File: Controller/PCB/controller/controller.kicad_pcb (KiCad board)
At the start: 2 copper layers, 99.1 x 99.1 mm, 64 parts, among them J1 nRF24L01_Conn, Q1 S9013, Q2 S9013, Q3 S9013, SW1 SW_SPDT, U1 Joystick, U2 Joystick, U3 ZSR330GTA, U4 LM358DR2G, U5 ZLDO1117G50TA

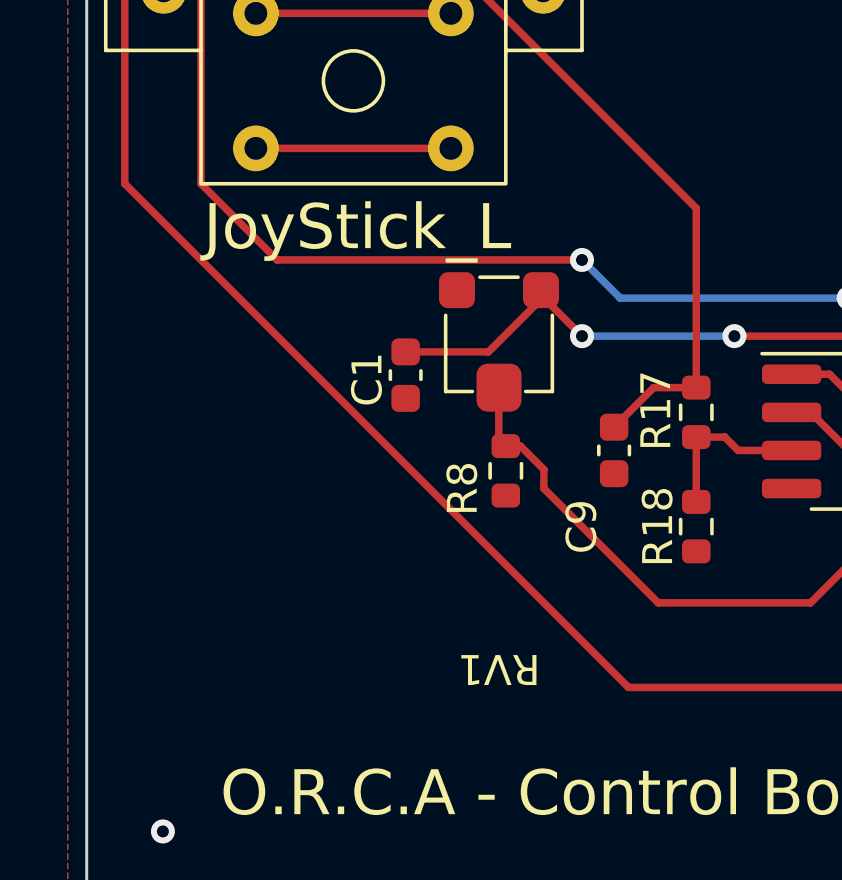
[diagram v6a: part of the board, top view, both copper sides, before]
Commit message: Change footprint of RV1 and update gerber files
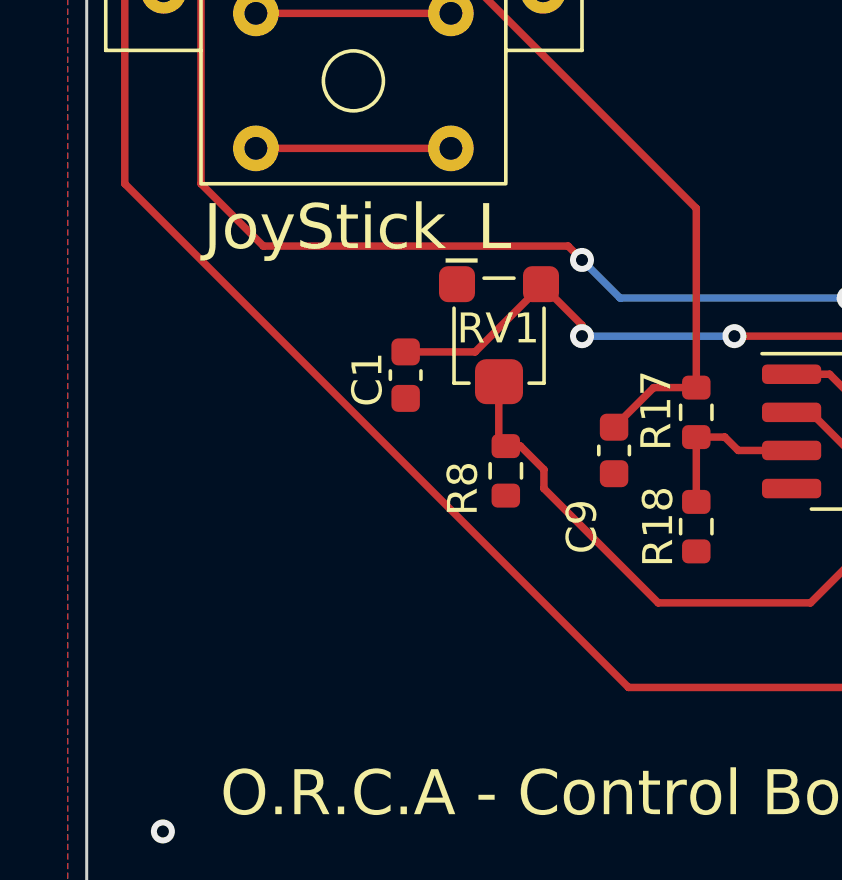
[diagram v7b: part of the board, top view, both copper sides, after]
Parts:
- RV1: footprint My_library:35WR100KLFTR -> My_library:Variable_Resistor
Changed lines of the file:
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@@
     )
   )
-  (footprint "My_library:35WR100KLFTR" (layer "F.Cu")
+  (footprint "My_library:Variable_Resistor" (layer "F.Cu")
     (at 120.423906 130.877391 180)
     (property "Sheetfile" "controller.kicad_sch")
     (property "Sheetname" "")
     (attr smd)
-    (fp_text reference "RV1" (at 0 -11.025 180 unlocked) (layer "F.SilkS")
-      (effects (font (size 1 1) (thickness 0.15)))
-    )
-    (fp_text value "20K" (at 0 -9.525 180 unlocked) (layer "F.Fab")
-      (effects (font (size 1 1) (thickness 0.15)))
-    )
-    (fp_text user "${REFERENCE}" (at 0 -7.62 180 unlocked) (layer "F.Fab")
-      (effects (font (size 1 1) (thickness 0.15)))
-    )
-    (fp_line (start -1.778 -1.778) (end -1.778 0.762) (layer "F.SilkS") (width 0.12))
-    (fp_line (start -0.889 -1.778) (end -1.778 -1.778) (layer "F.SilkS") (width 0.12))
-    (fp_line (start 0.889 -1.778) (end 1.778 -1.778) (layer "F.SilkS") (width 0.12))
-    (fp_line (start -0.635 2.032) (end 0.635 2.032) (layer "F.SilkS") (width 0.12))
-    (fp_line (start 1.778 -1.778) (end 1.778 0.762) (layer "F.SilkS") (width 0.12))
-    (pad "1" smd roundrect (at -1.4 1.6 180) (size 1.2 1.2) (layers "F.Cu" "F.Paste" "F.Mask") (roundrect_rratio 0.25)
+    (fp_text reference "RV1" (at 0.027906 0.321391 unlocked) (layer "F.SilkS")
+      (effects (font (size 1 1) (thickness 0.15)))
+    )
+    (fp_text value "20K" (at 0 -10.5 180 unlocked) (layer "F.Fab")
+      (effects (font (size 1 1) (thickness 0.15)))
+    )
+    (fp_text user "${REFERENCE}" (at 0 -9 180 unlocked) (layer "F.Fab")
+      (effects (font (size 1 1) (thickness 0.15)))
+    )
+    (fp_line (start 1.5 -1.5) (end 1.5 1) (layer "F.SilkS") (width 0.12))
+    (fp_line (start 0.5 2) (end -0.5 2) (layer "F.SilkS") (width 0.12))
+    (fp_line (start -1.5 1) (end -1.5 -1.5) (layer "F.SilkS") (width 0.12))
+    (fp_line (start 1 -1.5) (end 1.5 -1.5) (layer "F.SilkS") (width 0.12))
+    (fp_line (start -1.5 -1.5) (end -1 -1.5) (layer "F.SilkS") (width 0.12))
+    (pad "1" smd roundrect (at -1.4 1.8 180) (size 1.2 1.2) (layers "F.Cu" "F.Paste" "F.Mask") (roundrect_rratio 0.25)
       (net 19 "+5V") (pinfunction "1") (pintype "passive"))
-    (pad "2" smd roundrect (at 0 -1.65 180) (size 1.5 1.6) (layers "F.Cu" "F.Paste" "F.Mask") (roundrect_rratio 0.25)
+    (pad "2" smd roundrect (at 0 -1.45 180) (size 1.6 1.5) (layers "F.Cu" "F.Paste" "F.Mask") (roundrect_rratio 0.25)
       (net 59 "Net-(R8-Pad2)") (pinfunction "2") (pintype "passive"))
-    (pad "3" smd roundrect (at 1.4 1.6 180) (size 1.2 1.2) (layers "F.Cu" "F.Paste" "F.Mask") (roundrect_rratio 0.25)
+    (pad "3" smd roundrect (at 1.4 1.8 180) (size 1.2 1.2) (layers "F.Cu" "F.Paste" "F.Mask") (roundrect_rratio 0.25)
       (net 3 "Earth") (pinfunction "3") (pintype "passive"))
   )
@@
   (segment (start 147.311432 121.466444) (end 147.32 121.457876) (width 0.25) (layer "B.Cu") (net 6))
   (segment (start 133.985 127.635) (end 140.335 127.635) (width 0.25) (layer "F.Cu") (net 7))
+  (segment (start 112.568291 127.808291) (end 110.49 125.73) (width 0.25) (layer "F.Cu") (net 7))
   (segment (start 117.665 58.42) (end 121.92 62.675) (width 0.25) (layer "F.Cu") (net 7))
   (segment (start 132.08 129.54) (end 133.985 127.635) (width 0.25) (layer "F.Cu") (net 7))
   (segment (start 158.87 132.08) (end 160.14 133.35) (width 0.25) (layer "F.Cu") (net 7))
+  (segment (start 122.728291 127.808291) (end 112.568291 127.808291) (width 0.25) (layer "F.Cu") (net 7))
+  (segment (start 110.49 125.73) (end 110.49 96.52) (width 0.25) (layer "F.Cu") (net 7))
   (segment (start 110.49 96.52) (end 121.92 85.09) (width 0.25) (layer "F.Cu") (net 7))
-  (segment (start 110.49 125.73) (end 110.49 96.52) (width 0.25) (layer "F.Cu") (net 7))
   (segment (start 144.78 132.08) (end 158.87 132.08) (width 0.25) (layer "F.Cu") (net 7))
-  (segment (start 123.19 128.27) (end 113.03 128.27) (width 0.25) (layer "F.Cu") (net 7))
-  (segment (start 113.03 128.27) (end 110.49 125.73) (width 0.25) (layer "F.Cu") (net 7))
+  (segment (start 123.19 128.27) (end 122.728291 127.808291) (width 0.25) (layer "F.Cu") (net 7))
+  (segment (start 121.92 85.09) (end 121.92 83.82) (width 0.25) (layer "F.Cu") (net 7))
   (segment (start 121.92 62.675) (end 121.92 68.58) (width 0.25) (layer "F.Cu") (net 7))
-  (segment (start 121.92 85.09) (end 121.92 83.82) (width 0.25) (layer "F.Cu") (net 7))
   (segment (start 140.335 127.635) (end 144.78 132.08) (width 0.25) (layer "F.Cu") (net 7))
   (via (at 121.92 83.82) (size 0.8) (drill 0.4) (layers "F.Cu" "B.Cu") (net 7))
@@
   (segment (start 146.17 116.84) (end 147.44 118.11) (width 0.25) (layer "F.Cu") (net 18))
   (segment (start 204.844281 95.624281) (end 204.844281 133.124185) (width 1) (layer "F.Cu") (net 19))
+  (segment (start 117.311483 131.334748) (end 119.627279 131.334748) (width 0.25) (layer "F.Cu") (net 19))
   (segment (start 195.728466 142.24) (end 186.245 142.24) (width 1) (layer "F.Cu") (net 19))
   (segment (start 137.728928 133.918928) (end 135.89 132.08) (width 0.25) (layer "F.Cu") (net 19))
-  (segment (start 121.817202 129.437202) (end 123.19 130.81) (width 0.25) (layer "F.Cu") (net 19))
   (segment (start 202.095 84.11) (end 194.145 84.11) (width 1) (layer "F.Cu") (net 19))
   (segment (start 194.145 73.95) (end 202.095 73.95) (width 1) (layer "F.Cu") (net 19))
   (segment (start 204.47 74.93) (end 204.47 80.01) (width 1) (layer "F.Cu") (net 19))
+  (segment (start 123.19 130.443485) (end 123.19 130.81) (width 0.25) (layer "F.Cu") (net 19))
   (segment (start 202.095 94.27) (end 194.145 94.27) (width 1) (layer "F.Cu") (net 19))
   (segment (start 167.005 59.69) (end 167.005 57.785) (width 1) (layer "F.Cu") (net 19))
-  (segment (start 121.817202 129.27406) (end 121.817202 129.437202) (width 0.25) (layer "F.Cu") (net 19))
   (segment (start 204.47 86.36) (end 202.22 84.11) (width 1) (layer "F.Cu") (net 19))
   (segment (start 187.96 53.34) (end 173.190869 53.34) (width 1) (layer "F.Cu") (net 19))
@@
   (segment (start 111.76 70.3325) (end 113.751522 70.3325) (width 1) (layer "F.Cu") (net 19))
   (segment (start 124.55 54.215) (end 129.54 54.215) (width 1) (layer "F.Cu") (net 19))
+  (segment (start 121.687967 129.27406) (end 122.020575 129.27406) (width 0.25) (layer "F.Cu") (net 19))
   (segment (start 133.35 55.88) (end 138.992864 55.88) (width 1) (layer "F.Cu") (net 19))
   (segment (start 200.83 137.138466) (end 195.728466 142.24) (width 1) (layer "F.Cu") (net 19))
+  (segment (start 119.627279 131.334748) (end 121.687967 129.27406) (width 0.25) (layer "F.Cu") (net 19))
   (segment (start 173.190869 53.34) (end 170.18 56.350869) (width 1) (layer "F.Cu") (net 19))
   (segment (start 129.54 86.97) (end 129.54 90.665) (width 1) (layer "F.Cu") (net 19))
@@
   (segment (start 167.005 57.785) (end 168.439131 56.350869) (width 1) (layer "F.Cu") (net 19))
   (segment (start 161.028756 65.73838) (end 161.028756 65.666244) (width 1) (layer "F.Cu") (net 19))
-  (segment (start 120.072236 131.334748) (end 117.311483 131.334748) (width 0.25) (layer "F.Cu") (net 19))
   (segment (start 181.61 147.955) (end 154.94 147.955) (width 1) (layer "F.Cu") (net 19))
   (segment (start 202.095 73.95) (end 203.49 73.95) (width 1) (layer "F.Cu") (net 19))
   (segment (start 124.46 54.305) (end 110.16 54.305) (width 1) (layer "F.Cu") (net 19))
   (segment (start 203.49 94.27) (end 204.844281 95.624281) (width 1) (layer "F.Cu") (net 19))
-  (segment (start 121.817202 129.589782) (end 120.072236 131.334748) (width 0.25) (layer "F.Cu") (net 19))
   (segment (start 203.49 73.95) (end 204.47 74.93) (width 1) (layer "F.Cu") (net 19))
   (segment (start 202.095 94.27) (end 202.275 94.27) (width 1) (layer "F.Cu") (net 19))
@@
   (segment (start 129.54 54.215) (end 131.685 54.215) (width 1) (layer "F.Cu") (net 19))
   (segment (start 135.2525 132.08) (end 133.9825 130.81) (width 0.25) (layer "F.Cu") (net 19))
+  (segment (start 122.020575 129.27406) (end 123.19 130.443485) (width 0.25) (layer "F.Cu") (net 19))
   (segment (start 110.16 54.305) (end 109.22 55.245) (width 1) (layer "F.Cu") (net 19))
   (segment (start 137.728928 133.918928) (end 138.43 134.62) (width 0.25) (layer "F.Cu") (net 19))
@@
   (segment (start 150.495 138.43) (end 147.44 138.43) (width 1) (layer "F.Cu") (net 19))
   (segment (start 204.47 80.01) (end 202.095 82.385) (width 1) (layer "F.Cu") (net 19))
-  (segment (start 121.817202 129.27406) (end 121.817202 129.589782) (width 0.25) (layer "F.Cu") (net 19))
   (segment (start 194.145 59.525) (end 194.145 73.95) (width 1) (layer "F.Cu") (net 19))
   (segment (start 182.842977 146.722023) (end 181.61 147.955) (width 1) (layer "F.Cu") (net 19))

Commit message: Remake Gerber FIles
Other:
- board text added: "Luke Waller"
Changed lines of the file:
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@@
+    (effects (font (size 1.5 1.5) (thickness 0.3)))
+  )
+  (gr_text "Luke Waller\n" (at 116.205 146.05) (layer "F.SilkS")
     (effects (font (size 1.5 1.5) (thickness 0.3)))
   )
@@
     (effects (font (size 1.5 1.5) (thickness 0.3)))
   )
-  (gr_text "O.R.C.A - Control Board" (at 123.19 146.05) (layer "F.SilkS")
+  (gr_text "O.R.C.A - Control Board" (at 123.19 143.51) (layer "F.SilkS")
     (effects (font (size 1.5 1.5) (thickness 0.3)))
   )
